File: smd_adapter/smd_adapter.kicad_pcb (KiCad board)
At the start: 2 copper layers, 7.7 x 7.7 mm, 6 parts, among them J1 Conn_01x01_Pin, J2 Conn_01x01_Pin, J3 Conn_01x01_Pin, J4 Conn_01x01_Pin, J5 Conn_01x01_Pin, U2 MCP73831-5-OT

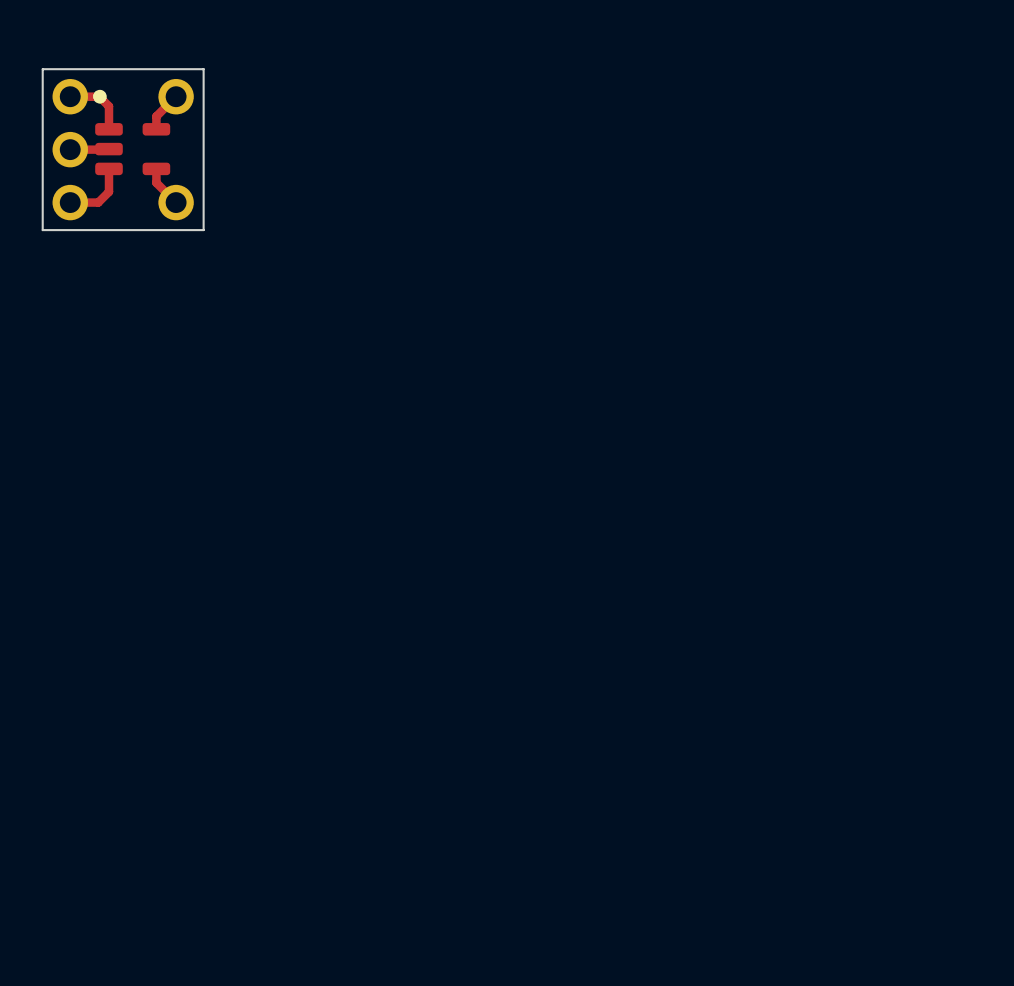
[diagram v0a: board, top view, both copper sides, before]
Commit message: Created adapter panel (5 x 5)
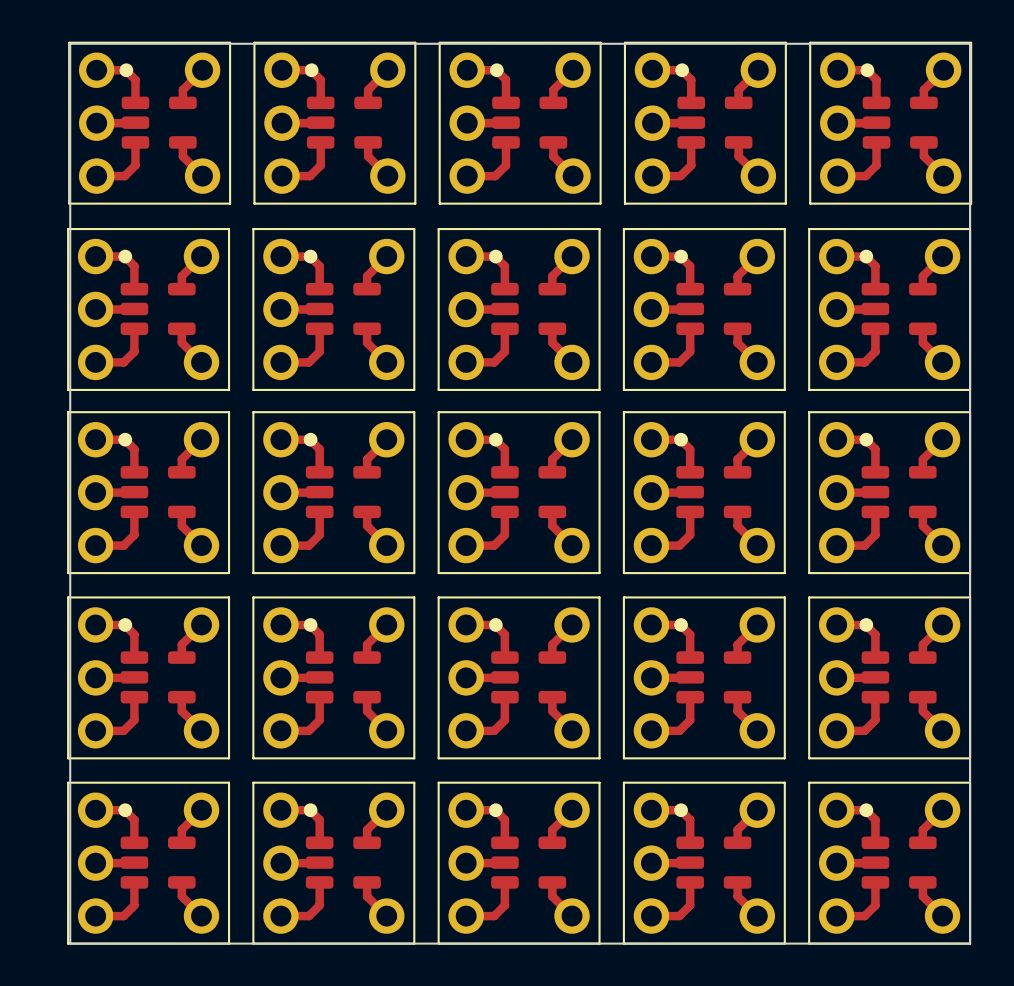
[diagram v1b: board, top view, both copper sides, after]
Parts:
- added J1: Conn_01x01_Pin, smd_adapter:pin_pad, F.Cu at (158.7, 143.5)
- added J1: Conn_01x01_Pin, smd_adapter:pin_pad, F.Cu at (194.3, 134.6)
- added J1: Conn_01x01_Pin, smd_adapter:pin_pad, F.Cu at (185.4, 134.6)
- added J1: Conn_01x01_Pin, smd_adapter:pin_pad, F.Cu at (185.4, 125.7)
- added J1: Conn_01x01_Pin, smd_adapter:pin_pad, F.Cu at (185.4, 108.0)
- added J1: Conn_01x01_Pin, smd_adapter:pin_pad, F.Cu at (167.6, 125.7)
- added J1: Conn_01x01_Pin, smd_adapter:pin_pad, F.Cu at (176.5, 143.5)
- added J1: Conn_01x01_Pin, smd_adapter:pin_pad, F.Cu at (176.5, 125.7)
- added J1: Conn_01x01_Pin, smd_adapter:pin_pad, F.Cu at (167.6, 143.5)
- added J1: Conn_01x01_Pin, smd_adapter:pin_pad, F.Cu at (176.5, 134.6)
- added J1: Conn_01x01_Pin, smd_adapter:pin_pad, F.Cu at (194.3, 125.7)
- added J1: Conn_01x01_Pin, smd_adapter:pin_pad, F.Cu at (167.6, 108.0)
- added J1: Conn_01x01_Pin, smd_adapter:pin_pad, F.Cu at (185.4, 116.9)
- added J1: Conn_01x01_Pin, smd_adapter:pin_pad, F.Cu at (158.7, 134.6)
- added J1: Conn_01x01_Pin, smd_adapter:pin_pad, F.Cu at (158.7, 125.7)
- added J1: Conn_01x01_Pin, smd_adapter:pin_pad, F.Cu at (194.3, 116.9)
- added J1: Conn_01x01_Pin, smd_adapter:pin_pad, F.Cu at (167.6, 134.6)
- added J1: Conn_01x01_Pin, smd_adapter:pin_pad, F.Cu at (194.3, 108.0)
- added J1: Conn_01x01_Pin, smd_adapter:pin_pad, F.Cu at (176.5, 116.9)
- added J1: Conn_01x01_Pin, smd_adapter:pin_pad, F.Cu at (167.6, 116.9)
- added J1: Conn_01x01_Pin, smd_adapter:pin_pad, F.Cu at (194.3, 143.5)
- added J1: Conn_01x01_Pin, smd_adapter:pin_pad, F.Cu at (185.4, 143.5)
- added J1: Conn_01x01_Pin, smd_adapter:pin_pad, F.Cu at (158.7, 116.9)
- added J1: Conn_01x01_Pin, smd_adapter:pin_pad, F.Cu at (176.5, 108.0)
- added J2: Conn_01x01_Pin, smd_adapter:pin_pad, F.Cu at (167.6, 129.5)
- added J2: Conn_01x01_Pin, smd_adapter:pin_pad, F.Cu at (158.7, 120.6)
- added J2: Conn_01x01_Pin, smd_adapter:pin_pad, F.Cu at (158.7, 111.8)
- added J2: Conn_01x01_Pin, smd_adapter:pin_pad, F.Cu at (167.6, 120.6)
- added J2: Conn_01x01_Pin, smd_adapter:pin_pad, F.Cu at (185.4, 102.9)
- added J2: Conn_01x01_Pin, smd_adapter:pin_pad, F.Cu at (194.3, 102.9)
- added J2: Conn_01x01_Pin, smd_adapter:pin_pad, F.Cu at (176.5, 138.4)
- added J2: Conn_01x01_Pin, smd_adapter:pin_pad, F.Cu at (176.5, 102.9)
- added J2: Conn_01x01_Pin, smd_adapter:pin_pad, F.Cu at (185.4, 120.6)
- added J2: Conn_01x01_Pin, smd_adapter:pin_pad, F.Cu at (158.7, 138.4)
- added J2: Conn_01x01_Pin, smd_adapter:pin_pad, F.Cu at (176.5, 111.8)
- added J2: Conn_01x01_Pin, smd_adapter:pin_pad, F.Cu at (167.6, 111.8)
- added J2: Conn_01x01_Pin, smd_adapter:pin_pad, F.Cu at (194.3, 120.6)
- added J2: Conn_01x01_Pin, smd_adapter:pin_pad, F.Cu at (176.5, 120.6)
- added J2: Conn_01x01_Pin, smd_adapter:pin_pad, F.Cu at (185.4, 129.5)
- added J2: Conn_01x01_Pin, smd_adapter:pin_pad, F.Cu at (167.6, 102.9)
- added J2: Conn_01x01_Pin, smd_adapter:pin_pad, F.Cu at (194.3, 111.8)
- added J2: Conn_01x01_Pin, smd_adapter:pin_pad, F.Cu at (158.7, 129.5)
- added J2: Conn_01x01_Pin, smd_adapter:pin_pad, F.Cu at (194.3, 129.5)
- added J2: Conn_01x01_Pin, smd_adapter:pin_pad, F.Cu at (185.4, 138.4)
- added J2: Conn_01x01_Pin, smd_adapter:pin_pad, F.Cu at (194.3, 138.4)
- added J2: Conn_01x01_Pin, smd_adapter:pin_pad, F.Cu at (176.5, 129.5)
- added J2: Conn_01x01_Pin, smd_adapter:pin_pad, F.Cu at (185.4, 111.8)
- added J2: Conn_01x01_Pin, smd_adapter:pin_pad, F.Cu at (167.6, 138.4)
- added J3: Conn_01x01_Pin, smd_adapter:pin_pad, F.Cu at (189.2, 114.4)
- added J3: Conn_01x01_Pin, smd_adapter:pin_pad, F.Cu at (153.6, 123.1)
- added J3: Conn_01x01_Pin, smd_adapter:pin_pad, F.Cu at (180.3, 140.9)
- added J3: Conn_01x01_Pin, smd_adapter:pin_pad, F.Cu at (162.6, 105.4)
- added J3: Conn_01x01_Pin, smd_adapter:pin_pad, F.Cu at (180.3, 114.4)
- added J3: Conn_01x01_Pin, smd_adapter:pin_pad, F.Cu at (171.4, 114.4)
- added J3: Conn_01x01_Pin, smd_adapter:pin_pad, F.Cu at (171.4, 132.0)
- added J3: Conn_01x01_Pin, smd_adapter:pin_pad, F.Cu at (189.2, 123.1)
- added J3: Conn_01x01_Pin, smd_adapter:pin_pad, F.Cu at (162.5, 132.0)
- added J3: Conn_01x01_Pin, smd_adapter:pin_pad, F.Cu at (162.5, 123.1)
- added J3: Conn_01x01_Pin, smd_adapter:pin_pad, F.Cu at (171.4, 105.4)
- added J3: Conn_01x01_Pin, smd_adapter:pin_pad, F.Cu at (180.3, 105.4)
- added J3: Conn_01x01_Pin, smd_adapter:pin_pad, F.Cu at (189.2, 140.9)
- added J3: Conn_01x01_Pin, smd_adapter:pin_pad, F.Cu at (153.6, 114.4)
- added J3: Conn_01x01_Pin, smd_adapter:pin_pad, F.Cu at (189.2, 105.4)
- added J3: Conn_01x01_Pin, smd_adapter:pin_pad, F.Cu at (162.5, 140.9)
- added J3: Conn_01x01_Pin, smd_adapter:pin_pad, F.Cu at (153.6, 132.0)
- added J3: Conn_01x01_Pin, smd_adapter:pin_pad, F.Cu at (162.5, 114.4)
- added J3: Conn_01x01_Pin, smd_adapter:pin_pad, F.Cu at (180.3, 123.1)
- added J3: Conn_01x01_Pin, smd_adapter:pin_pad, F.Cu at (171.4, 123.1)
- added J3: Conn_01x01_Pin, smd_adapter:pin_pad, F.Cu at (153.6, 140.9)
- added J3: Conn_01x01_Pin, smd_adapter:pin_pad, F.Cu at (189.2, 132.0)
- added J3: Conn_01x01_Pin, smd_adapter:pin_pad, F.Cu at (171.4, 140.9)
- added J3: Conn_01x01_Pin, smd_adapter:pin_pad, F.Cu at (180.3, 132.0)
- added J4: Conn_01x01_Pin, smd_adapter:pin_pad, F.Cu at (153.6, 138.4)
- added J4: Conn_01x01_Pin, smd_adapter:pin_pad, F.Cu at (171.4, 111.8)
- added J4: Conn_01x01_Pin, smd_adapter:pin_pad, F.Cu at (171.4, 120.6)
- added J4: Conn_01x01_Pin, smd_adapter:pin_pad, F.Cu at (171.4, 129.5)
- added J4: Conn_01x01_Pin, smd_adapter:pin_pad, F.Cu at (162.6, 102.9)
- added J4: Conn_01x01_Pin, smd_adapter:pin_pad, F.Cu at (162.5, 129.5)
- added J4: Conn_01x01_Pin, smd_adapter:pin_pad, F.Cu at (189.2, 138.4)
- added J4: Conn_01x01_Pin, smd_adapter:pin_pad, F.Cu at (153.6, 111.8)
- added J4: Conn_01x01_Pin, smd_adapter:pin_pad, F.Cu at (180.3, 120.6)
- added J4: Conn_01x01_Pin, smd_adapter:pin_pad, F.Cu at (171.4, 102.9)
- added J4: Conn_01x01_Pin, smd_adapter:pin_pad, F.Cu at (180.3, 138.4)
- added J4: Conn_01x01_Pin, smd_adapter:pin_pad, F.Cu at (189.2, 102.9)
- added J4: Conn_01x01_Pin, smd_adapter:pin_pad, F.Cu at (153.6, 120.6)
- added J4: Conn_01x01_Pin, smd_adapter:pin_pad, F.Cu at (180.3, 129.5)
- added J4: Conn_01x01_Pin, smd_adapter:pin_pad, F.Cu at (162.5, 120.6)
- added J4: Conn_01x01_Pin, smd_adapter:pin_pad, F.Cu at (180.3, 111.8)
- added J4: Conn_01x01_Pin, smd_adapter:pin_pad, F.Cu at (153.6, 129.5)
- added J4: Conn_01x01_Pin, smd_adapter:pin_pad, F.Cu at (189.2, 111.8)
- added J4: Conn_01x01_Pin, smd_adapter:pin_pad, F.Cu at (162.5, 111.8)
- added J4: Conn_01x01_Pin, smd_adapter:pin_pad, F.Cu at (189.2, 120.6)
- added J4: Conn_01x01_Pin, smd_adapter:pin_pad, F.Cu at (171.4, 138.4)
- added J4: Conn_01x01_Pin, smd_adapter:pin_pad, F.Cu at (189.2, 129.5)
- added J4: Conn_01x01_Pin, smd_adapter:pin_pad, F.Cu at (162.5, 138.4)
- added J4: Conn_01x01_Pin, smd_adapter:pin_pad, F.Cu at (180.3, 102.9)
- added J5: Conn_01x01_Pin, smd_adapter:pin_pad, F.Cu at (171.4, 116.9)
- added J5: Conn_01x01_Pin, smd_adapter:pin_pad, F.Cu at (153.6, 125.7)
- added J5: Conn_01x01_Pin, smd_adapter:pin_pad, F.Cu at (162.6, 108.0)
- added J5: Conn_01x01_Pin, smd_adapter:pin_pad, F.Cu at (189.2, 143.5)
- added J5: Conn_01x01_Pin, smd_adapter:pin_pad, F.Cu at (180.3, 143.5)
- added J5: Conn_01x01_Pin, smd_adapter:pin_pad, F.Cu at (153.6, 143.5)
- added J5: Conn_01x01_Pin, smd_adapter:pin_pad, F.Cu at (189.2, 134.6)
- added J5: Conn_01x01_Pin, smd_adapter:pin_pad, F.Cu at (171.4, 125.7)
- added J5: Conn_01x01_Pin, smd_adapter:pin_pad, F.Cu at (180.3, 134.6)
- added J5: Conn_01x01_Pin, smd_adapter:pin_pad, F.Cu at (189.2, 116.9)
- added J5: Conn_01x01_Pin, smd_adapter:pin_pad, F.Cu at (171.4, 134.6)
- added J5: Conn_01x01_Pin, smd_adapter:pin_pad, F.Cu at (153.6, 134.6)
- added J5: Conn_01x01_Pin, smd_adapter:pin_pad, F.Cu at (162.5, 143.5)
- added J5: Conn_01x01_Pin, smd_adapter:pin_pad, F.Cu at (180.3, 116.9)
- added J5: Conn_01x01_Pin, smd_adapter:pin_pad, F.Cu at (189.2, 108.0)
- added J5: Conn_01x01_Pin, smd_adapter:pin_pad, F.Cu at (171.4, 143.5)
- added J5: Conn_01x01_Pin, smd_adapter:pin_pad, F.Cu at (162.5, 116.9)
- added J5: Conn_01x01_Pin, smd_adapter:pin_pad, F.Cu at (180.3, 108.0)
- added J5: Conn_01x01_Pin, smd_adapter:pin_pad, F.Cu at (189.2, 125.7)
- added J5: Conn_01x01_Pin, smd_adapter:pin_pad, F.Cu at (171.4, 108.0)
- added J5: Conn_01x01_Pin, smd_adapter:pin_pad, F.Cu at (162.5, 125.7)
- added J5: Conn_01x01_Pin, smd_adapter:pin_pad, F.Cu at (180.3, 125.7)
- added J5: Conn_01x01_Pin, smd_adapter:pin_pad, F.Cu at (153.6, 116.9)
- added J5: Conn_01x01_Pin, smd_adapter:pin_pad, F.Cu at (162.5, 134.6)
- added U2: MCP73831-5-OT, smd_adapter:SOT-23-5, F.Cu at (156.6, 123.1)
- added U2: MCP73831-5-OT, smd_adapter:SOT-23-5, F.Cu at (156.6, 114.3)
- added U2: MCP73831-5-OT, smd_adapter:SOT-23-5, F.Cu at (183.3, 132.0)
- added U2: MCP73831-5-OT, smd_adapter:SOT-23-5, F.Cu at (165.6, 105.4)
- added U2: MCP73831-5-OT, smd_adapter:SOT-23-5, F.Cu at (183.3, 140.9)
- added U2: MCP73831-5-OT, smd_adapter:SOT-23-5, F.Cu at (156.6, 140.9)
- added U2: MCP73831-5-OT, smd_adapter:SOT-23-5, F.Cu at (183.3, 114.3)
- added U2: MCP73831-5-OT, smd_adapter:SOT-23-5, F.Cu at (192.2, 114.3)
- added U2: MCP73831-5-OT, smd_adapter:SOT-23-5, F.Cu at (174.4, 123.1)
- added U2: MCP73831-5-OT, smd_adapter:SOT-23-5, F.Cu at (192.2, 140.9)
- added U2: MCP73831-5-OT, smd_adapter:SOT-23-5, F.Cu at (174.4, 132.0)
- added U2: MCP73831-5-OT, smd_adapter:SOT-23-5, F.Cu at (192.2, 123.1)
- added U2: MCP73831-5-OT, smd_adapter:SOT-23-5, F.Cu at (165.5, 123.1)
- added U2: MCP73831-5-OT, smd_adapter:SOT-23-5, F.Cu at (165.5, 140.9)
- added U2: MCP73831-5-OT, smd_adapter:SOT-23-5, F.Cu at (174.4, 114.3)
- added U2: MCP73831-5-OT, smd_adapter:SOT-23-5, F.Cu at (192.2, 105.4)
- added U2: MCP73831-5-OT, smd_adapter:SOT-23-5, F.Cu at (165.5, 114.3)
- added U2: MCP73831-5-OT, smd_adapter:SOT-23-5, F.Cu at (183.3, 123.1)
- added U2: MCP73831-5-OT, smd_adapter:SOT-23-5, F.Cu at (165.5, 132.0)
- added U2: MCP73831-5-OT, smd_adapter:SOT-23-5, F.Cu at (174.4, 105.4)
- added U2: MCP73831-5-OT, smd_adapter:SOT-23-5, F.Cu at (183.3, 105.4)
- added U2: MCP73831-5-OT, smd_adapter:SOT-23-5, F.Cu at (192.2, 132.0)
- added U2: MCP73831-5-OT, smd_adapter:SOT-23-5, F.Cu at (174.4, 140.9)
- added U2: MCP73831-5-OT, smd_adapter:SOT-23-5, F.Cu at (156.6, 132.0)
- moved J1 1.80 mm to (158.8, 108.0)
- moved J2 1.80 mm to (158.8, 102.9)
- moved U2 1.80 mm to (156.7, 105.4)
- moved J3 1.80 mm to (153.7, 105.4)
- moved J4 1.80 mm to (153.7, 102.9)
- moved J5 1.80 mm to (153.7, 108.0)
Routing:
- net Net-(J5-Pin_1): track 3.17 -> 79.4 mm
- net Net-(J4-Pin_1): track 3.15 -> 78.8 mm
- net Net-(J1-Pin_1): track 2.01 -> 50.2 mm
- net Net-(J2-Pin_1): track 1.96 -> 48.9 mm
- net Net-(J3-Pin_1): track 1.87 -> 46.8 mm
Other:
- board size 7.7 x 7.7 mm -> 43.2 x 43.2 mm

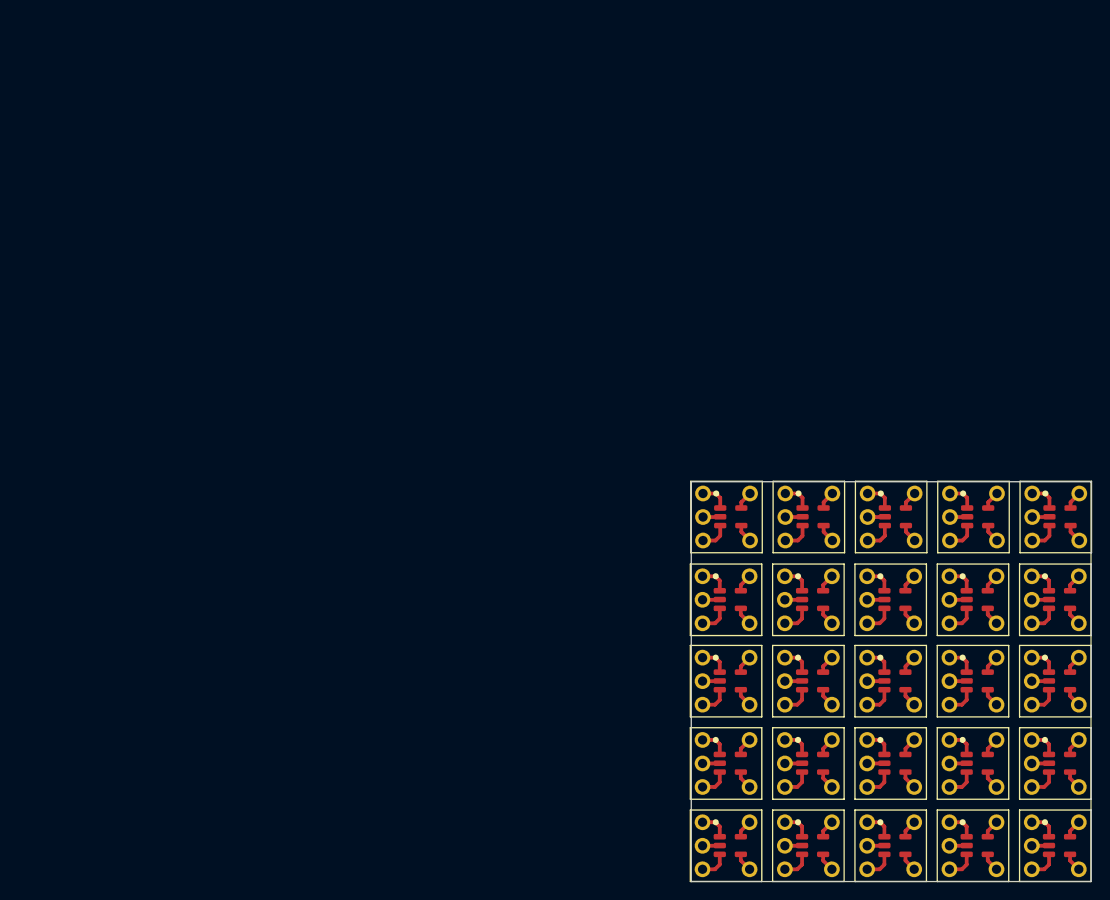
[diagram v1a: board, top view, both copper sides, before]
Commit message: Completed the layout of the smd adapters (5 kinds)
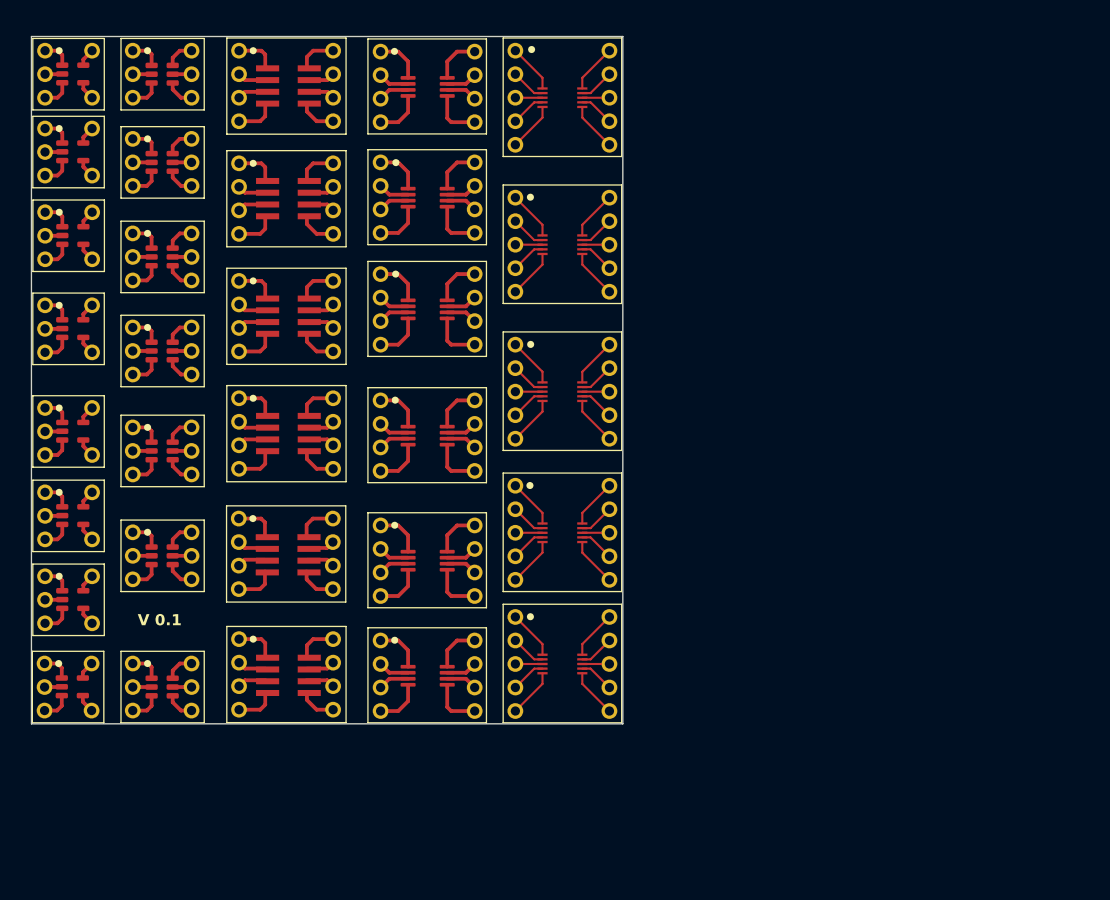
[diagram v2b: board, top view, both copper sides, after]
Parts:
- removed the J1 at (158.7, 143.5)
- removed the J1 at (194.3, 134.6)
- removed the J1 at (185.4, 134.6)
- removed the J1 at (185.4, 125.7)
- removed the J1 at (185.4, 108.0)
- removed the J1 at (167.6, 125.7)
- removed the J1 at (176.5, 143.5)
- removed the J1 at (176.5, 125.7)
- removed the J1 at (167.6, 143.5)
- removed the J1 at (176.5, 134.6)
- removed the J1 at (194.3, 125.7)
- removed the J1 at (167.6, 108.0)
- removed the J1 at (185.4, 116.9)
- removed the J1 at (158.7, 134.6)
- removed the J1 at (158.7, 125.7)
- removed the J1 at (194.3, 116.9)
- removed the J1 at (167.6, 134.6)
- removed the J1 at (194.3, 108.0)
- removed the J1 at (176.5, 116.9)
- removed the J1 at (167.6, 116.9)
- removed the J1 at (194.3, 143.5)
- removed the J1 at (185.4, 143.5)
- removed the J1 at (158.7, 116.9)
- removed the J1 at (176.5, 108.0)
- removed the J2 at (167.6, 129.5)
- removed the J2 at (158.7, 120.6)
- removed the J2 at (158.7, 111.8)
- removed the J2 at (167.6, 120.6)
- removed the J2 at (185.4, 102.9)
- removed the J2 at (194.3, 102.9)
- removed the J2 at (176.5, 138.4)
- removed the J2 at (176.5, 102.9)
- removed the J2 at (185.4, 120.6)
- removed the J2 at (158.7, 138.4)
- removed the J2 at (176.5, 111.8)
- removed the J2 at (167.6, 111.8)
- removed the J2 at (194.3, 120.6)
- removed the J2 at (176.5, 120.6)
- removed the J2 at (185.4, 129.5)
- removed the J2 at (167.6, 102.9)
- removed the J2 at (194.3, 111.8)
- removed the J2 at (158.7, 129.5)
- removed the J2 at (194.3, 129.5)
- removed the J2 at (185.4, 138.4)
- removed the J2 at (194.3, 138.4)
- removed the J2 at (176.5, 129.5)
- removed the J2 at (185.4, 111.8)
- removed the J2 at (167.6, 138.4)
- removed the J3 at (189.2, 114.4)
- removed the J3 at (153.6, 123.1)
- removed the J3 at (180.3, 140.9)
- removed the J3 at (162.6, 105.4)
- removed the J3 at (180.3, 114.4)
- removed the J3 at (171.4, 114.4)
- removed the J3 at (171.4, 132.0)
- removed the J3 at (189.2, 123.1)
- removed the J3 at (162.5, 132.0)
- removed the J3 at (162.5, 123.1)
- removed the J3 at (171.4, 105.4)
- removed the J3 at (180.3, 105.4)
- removed the J3 at (189.2, 140.9)
- removed the J3 at (153.6, 114.4)
- removed the J3 at (189.2, 105.4)
- removed the J3 at (162.5, 140.9)
- removed the J3 at (153.6, 132.0)
- removed the J3 at (162.5, 114.4)
- removed the J3 at (180.3, 123.1)
- removed the J3 at (171.4, 123.1)
- removed the J3 at (153.6, 140.9)
- removed the J3 at (189.2, 132.0)
- removed the J3 at (171.4, 140.9)
- removed the J3 at (180.3, 132.0)
- removed the J4 at (153.6, 138.4)
- removed the J4 at (171.4, 111.8)
- removed the J4 at (171.4, 120.6)
- removed the J4 at (171.4, 129.5)
- removed the J4 at (162.6, 102.9)
- removed the J4 at (162.5, 129.5)
- removed the J4 at (189.2, 138.4)
- removed the J4 at (153.6, 111.8)
- removed the J4 at (180.3, 120.6)
- removed the J4 at (171.4, 102.9)
- removed the J4 at (180.3, 138.4)
- removed the J4 at (189.2, 102.9)
- removed the J4 at (153.6, 120.6)
- removed the J4 at (180.3, 129.5)
- removed the J4 at (162.5, 120.6)
- removed the J4 at (180.3, 111.8)
- removed the J4 at (153.6, 129.5)
- removed the J4 at (189.2, 111.8)
- removed the J4 at (162.5, 111.8)
- removed the J4 at (189.2, 120.6)
- removed the J4 at (171.4, 138.4)
- removed the J4 at (189.2, 129.5)
- removed the J4 at (162.5, 138.4)
- removed the J4 at (180.3, 102.9)
- removed the J5 at (171.4, 116.9)
- removed the J5 at (153.6, 125.7)
- removed the J5 at (162.6, 108.0)
- removed the J5 at (189.2, 143.5)
- removed the J5 at (180.3, 143.5)
- removed the J5 at (153.6, 143.5)
- removed the J5 at (189.2, 134.6)
- removed the J5 at (171.4, 125.7)
- removed the J5 at (180.3, 134.6)
- removed the J5 at (189.2, 116.9)
- removed the J5 at (171.4, 134.6)
- removed the J5 at (153.6, 134.6)
- removed the J5 at (162.5, 143.5)
- removed the J5 at (180.3, 116.9)
- removed the J5 at (189.2, 108.0)
- removed the J5 at (171.4, 143.5)
- removed the J5 at (162.5, 116.9)
- removed the J5 at (180.3, 108.0)
- removed the J5 at (189.2, 125.7)
- removed the J5 at (171.4, 108.0)
- removed the J5 at (162.5, 125.7)
- removed the J5 at (180.3, 125.7)
- removed the J5 at (153.6, 116.9)
- removed the J5 at (162.5, 134.6)
- removed the U2 at (156.6, 123.1)
- removed the U2 at (156.6, 114.3)
- removed the U2 at (183.3, 132.0)
- removed the U2 at (165.6, 105.4)
- removed the U2 at (183.3, 140.9)
- removed the U2 at (156.6, 140.9)
- removed the U2 at (183.3, 114.3)
- removed the U2 at (192.2, 114.3)
- removed the U2 at (174.4, 123.1)
- removed the U2 at (192.2, 140.9)
- removed the U2 at (174.4, 132.0)
- removed the U2 at (192.2, 123.1)
- removed the U2 at (165.5, 123.1)
- removed the U2 at (165.5, 140.9)
- removed the U2 at (174.4, 114.3)
- removed the U2 at (192.2, 105.4)
- removed the U2 at (165.5, 114.3)
- removed the U2 at (183.3, 123.1)
- removed the U2 at (165.5, 132.0)
- removed the U2 at (174.4, 105.4)
- removed the U2 at (183.3, 105.4)
- removed the U2 at (192.2, 132.0)
- removed the U2 at (174.4, 140.9)
- removed the U2 at (156.6, 132.0)
- added J1: Conn_01x01_Pin, smd_adapter:pin_pad, F.Cu at (87.7, 107.8)
- added J1: Conn_01x01_Pin, smd_adapter:pin_pad, F.Cu at (87.6, 126.3)
- added J1: Conn_01x01_Pin, smd_adapter:pin_pad, F.Cu at (87.7, 87.6)
- added J1: Conn_01x01_Pin, smd_adapter:pin_pad, F.Cu at (87.7, 68.5)
- added J1: Conn_01x01_Pin, smd_adapter:pin_pad, F.Cu at (87.7, 98.7)
- added J1: Conn_01x01_Pin, smd_adapter:pin_pad, F.Cu at (87.7, 116.9)
- added J1: Conn_01x01_Pin, smd_adapter:pin_pad, F.Cu at (87.7, 77.6)
- added J10: Conn_01x01_Pin, smd_adapter:pin_pad, F.Cu at (113.7, 105.6)
- added J10: Conn_01x01_Pin, smd_adapter:pin_pad, F.Cu at (113.7, 118.6)
- added J10: Conn_01x01_Pin, smd_adapter:pin_pad, F.Cu at (113.7, 79.9)
- added J10: Conn_01x01_Pin, smd_adapter:pin_pad, F.Cu at (113.7, 92.6)
- added J10: Conn_01x01_Pin, smd_adapter:pin_pad, F.Cu at (113.7, 55.0)
- added J10: Conn_01x01_Pin, smd_adapter:pin_pad, F.Cu at (113.7, 67.2)
- added J11: Conn_01x01_Pin, smd_adapter:pin_pad, F.Cu at (113.7, 82.4)
- added J11: Conn_01x01_Pin, smd_adapter:pin_pad, F.Cu at (113.7, 95.1)
- added J11: Conn_01x01_Pin, smd_adapter:pin_pad, F.Cu at (113.7, 57.6)
- added J11: Conn_01x01_Pin, smd_adapter:pin_pad, F.Cu at (113.7, 69.7)
- added J11: Conn_01x01_Pin, smd_adapter:pin_pad, F.Cu at (113.7, 121.1)
- added J11: Conn_01x01_Pin, smd_adapter:pin_pad, F.Cu at (113.7, 108.1)
- added J12: Conn_01x01_Pin, smd_adapter:pin_pad, F.Cu at (113.7, 110.7)
- added J12: Conn_01x01_Pin, smd_adapter:pin_pad, F.Cu at (113.7, 60.1)
- added J12: Conn_01x01_Pin, smd_adapter:pin_pad, F.Cu at (113.7, 85.0)
- added J12: Conn_01x01_Pin, smd_adapter:pin_pad, F.Cu at (113.7, 97.7)
- added J12: Conn_01x01_Pin, smd_adapter:pin_pad, F.Cu at (113.7, 72.3)
- added J12: Conn_01x01_Pin, smd_adapter:pin_pad, F.Cu at (113.7, 123.7)
- added J13: Conn_01x01_Pin, smd_adapter:pin_pad, F.Cu at (113.7, 113.2)
- added J13: Conn_01x01_Pin, smd_adapter:pin_pad, F.Cu at (113.7, 87.5)
- added J13: Conn_01x01_Pin, smd_adapter:pin_pad, F.Cu at (113.7, 62.7)
- added J13: Conn_01x01_Pin, smd_adapter:pin_pad, F.Cu at (113.7, 74.8)
- added J13: Conn_01x01_Pin, smd_adapter:pin_pad, F.Cu at (113.7, 100.2)
- added J13: Conn_01x01_Pin, smd_adapter:pin_pad, F.Cu at (113.7, 126.2)
- added J14: Conn_01x01_Pin, smd_adapter:pin_pad, F.Cu at (92.1, 121.2)
- added J14: Conn_01x01_Pin, smd_adapter:pin_pad, F.Cu at (92.1, 64.6)
- added J14: Conn_01x01_Pin, smd_adapter:pin_pad, F.Cu at (92.1, 95.7)
- added J14: Conn_01x01_Pin, smd_adapter:pin_pad, F.Cu at (92.1, 107.1)
- added J14: Conn_01x01_Pin, smd_adapter:pin_pad, F.Cu at (92.1, 55.0)
- added J14: Conn_01x01_Pin, smd_adapter:pin_pad, F.Cu at (92.1, 74.8)
- added J14: Conn_01x01_Pin, smd_adapter:pin_pad, F.Cu at (92.1, 84.9)
- added J15: Conn_01x01_Pin, smd_adapter:pin_pad, F.Cu at (92.1, 98.3)
- added J15: Conn_01x01_Pin, smd_adapter:pin_pad, F.Cu at (92.1, 57.6)
- added J15: Conn_01x01_Pin, smd_adapter:pin_pad, F.Cu at (92.1, 109.6)
- added J15: Conn_01x01_Pin, smd_adapter:pin_pad, F.Cu at (92.1, 123.8)
- added J15: Conn_01x01_Pin, smd_adapter:pin_pad, F.Cu at (92.1, 77.3)
- added J15: Conn_01x01_Pin, smd_adapter:pin_pad, F.Cu at (92.1, 87.5)
- added J15: Conn_01x01_Pin, smd_adapter:pin_pad, F.Cu at (92.1, 67.1)
- added J16: Conn_01x01_Pin, smd_adapter:pin_pad, F.Cu at (92.1, 112.1)
- added J16: Conn_01x01_Pin, smd_adapter:pin_pad, F.Cu at (92.1, 126.3)
- added J16: Conn_01x01_Pin, smd_adapter:pin_pad, F.Cu at (92.1, 69.6)
- added J16: Conn_01x01_Pin, smd_adapter:pin_pad, F.Cu at (92.1, 90.0)
- added J16: Conn_01x01_Pin, smd_adapter:pin_pad, F.Cu at (92.1, 79.9)
- added J16: Conn_01x01_Pin, smd_adapter:pin_pad, F.Cu at (92.1, 60.1)
- added J16: Conn_01x01_Pin, smd_adapter:pin_pad, F.Cu at (92.1, 100.8)
- added J17: Conn_01x01_Pin, smd_adapter:pin_pad, F.Cu at (98.4, 74.8)
- added J17: Conn_01x01_Pin, smd_adapter:pin_pad, F.Cu at (98.4, 121.2)
- added J17: Conn_01x01_Pin, smd_adapter:pin_pad, F.Cu at (98.4, 55.0)
- added J17: Conn_01x01_Pin, smd_adapter:pin_pad, F.Cu at (98.4, 95.7)
- added J17: Conn_01x01_Pin, smd_adapter:pin_pad, F.Cu at (98.4, 84.9)
- added J17: Conn_01x01_Pin, smd_adapter:pin_pad, F.Cu at (98.4, 64.6)
- added J17: Conn_01x01_Pin, smd_adapter:pin_pad, F.Cu at (98.4, 107.1)
- added J18: Conn_01x01_Pin, smd_adapter:pin_pad, F.Cu at (98.4, 109.6)
- added J18: Conn_01x01_Pin, smd_adapter:pin_pad, F.Cu at (98.4, 57.6)
- added J18: Conn_01x01_Pin, smd_adapter:pin_pad, F.Cu at (98.4, 77.3)
- added J18: Conn_01x01_Pin, smd_adapter:pin_pad, F.Cu at (98.4, 98.3)
- added J18: Conn_01x01_Pin, smd_adapter:pin_pad, F.Cu at (98.4, 123.8)
- added J18: Conn_01x01_Pin, smd_adapter:pin_pad, F.Cu at (98.4, 87.5)
- added J18: Conn_01x01_Pin, smd_adapter:pin_pad, F.Cu at (98.4, 67.1)
- added J19: Conn_01x01_Pin, smd_adapter:pin_pad, F.Cu at (98.4, 100.8)
- added J19: Conn_01x01_Pin, smd_adapter:pin_pad, F.Cu at (98.4, 126.3)
- added J19: Conn_01x01_Pin, smd_adapter:pin_pad, F.Cu at (98.4, 79.9)
- added J19: Conn_01x01_Pin, smd_adapter:pin_pad, F.Cu at (98.4, 60.1)
- added J19: Conn_01x01_Pin, smd_adapter:pin_pad, F.Cu at (98.4, 69.6)
- added J19: Conn_01x01_Pin, smd_adapter:pin_pad, F.Cu at (98.4, 90.0)
- added J19: Conn_01x01_Pin, smd_adapter:pin_pad, F.Cu at (98.4, 112.1)
- added J2: Conn_01x01_Pin, smd_adapter:pin_pad, F.Cu at (87.7, 72.5)
- added J2: Conn_01x01_Pin, smd_adapter:pin_pad, F.Cu at (87.7, 82.5)
- added J2: Conn_01x01_Pin, smd_adapter:pin_pad, F.Cu at (87.7, 63.4)
- added J2: Conn_01x01_Pin, smd_adapter:pin_pad, F.Cu at (87.7, 93.6)
- added J2: Conn_01x01_Pin, smd_adapter:pin_pad, F.Cu at (87.6, 121.2)
- added J2: Conn_01x01_Pin, smd_adapter:pin_pad, F.Cu at (87.7, 102.7)
- added J2: Conn_01x01_Pin, smd_adapter:pin_pad, F.Cu at (87.7, 111.8)
- added J20: Conn_01x01_Pin, smd_adapter:pin_pad, F.Cu at (118.8, 79.2)
- added J20: Conn_01x01_Pin, smd_adapter:pin_pad, F.Cu at (118.8, 55.1)
- added J20: Conn_01x01_Pin, smd_adapter:pin_pad, F.Cu at (118.8, 67.1)
- added J20: Conn_01x01_Pin, smd_adapter:pin_pad, F.Cu at (118.8, 118.7)
- added J20: Conn_01x01_Pin, smd_adapter:pin_pad, F.Cu at (118.8, 106.3)
- added J20: Conn_01x01_Pin, smd_adapter:pin_pad, F.Cu at (118.8, 92.8)
- added J21: Conn_01x01_Pin, smd_adapter:pin_pad, F.Cu at (118.8, 81.7)
- added J21: Conn_01x01_Pin, smd_adapter:pin_pad, F.Cu at (118.8, 57.7)
- added J21: Conn_01x01_Pin, smd_adapter:pin_pad, F.Cu at (118.8, 69.6)
- added J21: Conn_01x01_Pin, smd_adapter:pin_pad, F.Cu at (118.8, 108.9)
- added J21: Conn_01x01_Pin, smd_adapter:pin_pad, F.Cu at (118.8, 95.4)
- added J21: Conn_01x01_Pin, smd_adapter:pin_pad, F.Cu at (118.8, 121.3)
- added J22: Conn_01x01_Pin, smd_adapter:pin_pad, F.Cu at (118.8, 123.8)
- added J22: Conn_01x01_Pin, smd_adapter:pin_pad, F.Cu at (118.8, 111.4)
- added J22: Conn_01x01_Pin, smd_adapter:pin_pad, F.Cu at (118.8, 60.2)
- added J22: Conn_01x01_Pin, smd_adapter:pin_pad, F.Cu at (118.8, 97.9)
- added J22: Conn_01x01_Pin, smd_adapter:pin_pad, F.Cu at (118.8, 84.3)
- added J22: Conn_01x01_Pin, smd_adapter:pin_pad, F.Cu at (118.8, 72.2)
- added J23: Conn_01x01_Pin, smd_adapter:pin_pad, F.Cu at (118.8, 62.8)
- added J23: Conn_01x01_Pin, smd_adapter:pin_pad, F.Cu at (118.8, 126.4)
- added J23: Conn_01x01_Pin, smd_adapter:pin_pad, F.Cu at (118.8, 74.7)
- added J23: Conn_01x01_Pin, smd_adapter:pin_pad, F.Cu at (118.8, 86.8)
- added J23: Conn_01x01_Pin, smd_adapter:pin_pad, F.Cu at (118.8, 100.4)
- added J23: Conn_01x01_Pin, smd_adapter:pin_pad, F.Cu at (118.8, 113.9)
- added J24: Conn_01x01_Pin, smd_adapter:pin_pad, F.Cu at (129.0, 118.7)
- added J24: Conn_01x01_Pin, smd_adapter:pin_pad, F.Cu at (129.0, 55.1)
- added J24: Conn_01x01_Pin, smd_adapter:pin_pad, F.Cu at (129.0, 67.1)
- added J24: Conn_01x01_Pin, smd_adapter:pin_pad, F.Cu at (129.0, 106.3)
- added J24: Conn_01x01_Pin, smd_adapter:pin_pad, F.Cu at (129.0, 79.2)
- added J24: Conn_01x01_Pin, smd_adapter:pin_pad, F.Cu at (129.0, 92.8)
- added J25: Conn_01x01_Pin, smd_adapter:pin_pad, F.Cu at (129.0, 81.7)
- added J25: Conn_01x01_Pin, smd_adapter:pin_pad, F.Cu at (129.0, 95.4)
- added J25: Conn_01x01_Pin, smd_adapter:pin_pad, F.Cu at (129.0, 57.7)
- added J25: Conn_01x01_Pin, smd_adapter:pin_pad, F.Cu at (129.0, 69.6)
- added J25: Conn_01x01_Pin, smd_adapter:pin_pad, F.Cu at (129.0, 121.3)
- added J25: Conn_01x01_Pin, smd_adapter:pin_pad, F.Cu at (129.0, 108.9)
- added J26: Conn_01x01_Pin, smd_adapter:pin_pad, F.Cu at (129.0, 123.8)
- added J26: Conn_01x01_Pin, smd_adapter:pin_pad, F.Cu at (129.0, 97.9)
- added J26: Conn_01x01_Pin, smd_adapter:pin_pad, F.Cu at (129.0, 72.2)
- added J26: Conn_01x01_Pin, smd_adapter:pin_pad, F.Cu at (129.0, 111.4)
- added J26: Conn_01x01_Pin, smd_adapter:pin_pad, F.Cu at (129.0, 60.2)
- added J26: Conn_01x01_Pin, smd_adapter:pin_pad, F.Cu at (129.0, 84.3)
- added J27: Conn_01x01_Pin, smd_adapter:pin_pad, F.Cu at (129.0, 86.8)
- added J27: Conn_01x01_Pin, smd_adapter:pin_pad, F.Cu at (129.0, 126.4)
- added J27: Conn_01x01_Pin, smd_adapter:pin_pad, F.Cu at (129.0, 74.7)
- added J27: Conn_01x01_Pin, smd_adapter:pin_pad, F.Cu at (129.0, 113.9)
- added J27: Conn_01x01_Pin, smd_adapter:pin_pad, F.Cu at (129.0, 62.8)
- added J27: Conn_01x01_Pin, smd_adapter:pin_pad, F.Cu at (129.0, 100.4)
- added J28: Conn_01x01_Pin, smd_adapter:pin_pad, F.Cu at (133.4, 70.9)
- added J28: Conn_01x01_Pin, smd_adapter:pin_pad, F.Cu at (133.4, 55.0)
- added J28: Conn_01x01_Pin, smd_adapter:pin_pad, F.Cu at (133.4, 86.8)
- added J28: Conn_01x01_Pin, smd_adapter:pin_pad, F.Cu at (133.4, 116.2)
- added J28: Conn_01x01_Pin, smd_adapter:pin_pad, F.Cu at (133.4, 102.0)
- added J29: Conn_01x01_Pin, smd_adapter:pin_pad, F.Cu at (133.4, 104.6)
- added J29: Conn_01x01_Pin, smd_adapter:pin_pad, F.Cu at (133.4, 118.7)
- added J29: Conn_01x01_Pin, smd_adapter:pin_pad, F.Cu at (133.4, 73.5)
- added J29: Conn_01x01_Pin, smd_adapter:pin_pad, F.Cu at (133.4, 89.3)
- added J29: Conn_01x01_Pin, smd_adapter:pin_pad, F.Cu at (133.4, 57.6)
- added J3: Conn_01x01_Pin, smd_adapter:pin_pad, F.Cu at (82.6, 96.2)
- added J3: Conn_01x01_Pin, smd_adapter:pin_pad, F.Cu at (82.6, 114.4)
- added J3: Conn_01x01_Pin, smd_adapter:pin_pad, F.Cu at (82.6, 75.0)
- added J3: Conn_01x01_Pin, smd_adapter:pin_pad, F.Cu at (82.6, 66.0)
- added J3: Conn_01x01_Pin, smd_adapter:pin_pad, F.Cu at (82.5, 123.8)
- added J3: Conn_01x01_Pin, smd_adapter:pin_pad, F.Cu at (82.6, 105.3)
- added J3: Conn_01x01_Pin, smd_adapter:pin_pad, F.Cu at (82.6, 85.1)
- added J30: Conn_01x01_Pin, smd_adapter:pin_pad, F.Cu at (133.4, 107.1)
- added J30: Conn_01x01_Pin, smd_adapter:pin_pad, F.Cu at (133.4, 91.9)
- added J30: Conn_01x01_Pin, smd_adapter:pin_pad, F.Cu at (133.4, 121.3)
- added J30: Conn_01x01_Pin, smd_adapter:pin_pad, F.Cu at (133.4, 60.1)
- added J30: Conn_01x01_Pin, smd_adapter:pin_pad, F.Cu at (133.4, 76.0)
- added J31: Conn_01x01_Pin, smd_adapter:pin_pad, F.Cu at (133.4, 109.7)
- added J31: Conn_01x01_Pin, smd_adapter:pin_pad, F.Cu at (133.4, 123.8)
- added J31: Conn_01x01_Pin, smd_adapter:pin_pad, F.Cu at (133.4, 94.4)
- added J31: Conn_01x01_Pin, smd_adapter:pin_pad, F.Cu at (133.4, 78.5)
- added J31: Conn_01x01_Pin, smd_adapter:pin_pad, F.Cu at (133.4, 62.7)
- added J32: Conn_01x01_Pin, smd_adapter:pin_pad, F.Cu at (133.4, 81.1)
- added J32: Conn_01x01_Pin, smd_adapter:pin_pad, F.Cu at (133.4, 126.4)
- added J32: Conn_01x01_Pin, smd_adapter:pin_pad, F.Cu at (133.4, 112.2)
- added J32: Conn_01x01_Pin, smd_adapter:pin_pad, F.Cu at (133.4, 65.2)
- added J32: Conn_01x01_Pin, smd_adapter:pin_pad, F.Cu at (133.4, 97.0)
- added J33: Conn_01x01_Pin, smd_adapter:pin_pad, F.Cu at (143.6, 55.0)
- added J33: Conn_01x01_Pin, smd_adapter:pin_pad, F.Cu at (143.6, 102.0)
- added J33: Conn_01x01_Pin, smd_adapter:pin_pad, F.Cu at (143.6, 116.2)
- added J33: Conn_01x01_Pin, smd_adapter:pin_pad, F.Cu at (143.6, 70.9)
- added J33: Conn_01x01_Pin, smd_adapter:pin_pad, F.Cu at (143.6, 86.8)
- added J34: Conn_01x01_Pin, smd_adapter:pin_pad, F.Cu at (143.6, 57.6)
- added J34: Conn_01x01_Pin, smd_adapter:pin_pad, F.Cu at (143.6, 118.7)
- added J34: Conn_01x01_Pin, smd_adapter:pin_pad, F.Cu at (143.6, 104.6)
- added J34: Conn_01x01_Pin, smd_adapter:pin_pad, F.Cu at (143.6, 89.3)
- added J34: Conn_01x01_Pin, smd_adapter:pin_pad, F.Cu at (143.6, 73.5)
- added J35: Conn_01x01_Pin, smd_adapter:pin_pad, F.Cu at (143.6, 60.1)
- added J35: Conn_01x01_Pin, smd_adapter:pin_pad, F.Cu at (143.6, 121.3)
- added J35: Conn_01x01_Pin, smd_adapter:pin_pad, F.Cu at (143.6, 91.9)
- added J35: Conn_01x01_Pin, smd_adapter:pin_pad, F.Cu at (143.6, 107.1)
- added J35: Conn_01x01_Pin, smd_adapter:pin_pad, F.Cu at (143.6, 76.0)
- added J36: Conn_01x01_Pin, smd_adapter:pin_pad, F.Cu at (143.6, 78.5)
- added J36: Conn_01x01_Pin, smd_adapter:pin_pad, F.Cu at (143.6, 109.7)
- added J36: Conn_01x01_Pin, smd_adapter:pin_pad, F.Cu at (143.6, 123.8)
- added J36: Conn_01x01_Pin, smd_adapter:pin_pad, F.Cu at (143.6, 62.7)
- added J36: Conn_01x01_Pin, smd_adapter:pin_pad, F.Cu at (143.6, 94.4)
- added J37: Conn_01x01_Pin, smd_adapter:pin_pad, F.Cu at (143.6, 112.2)
- added J37: Conn_01x01_Pin, smd_adapter:pin_pad, F.Cu at (143.6, 126.4)
- added J37: Conn_01x01_Pin, smd_adapter:pin_pad, F.Cu at (143.6, 97.0)
- added J37: Conn_01x01_Pin, smd_adapter:pin_pad, F.Cu at (143.6, 81.1)
- added J37: Conn_01x01_Pin, smd_adapter:pin_pad, F.Cu at (143.6, 65.2)
- added J4: Conn_01x01_Pin, smd_adapter:pin_pad, F.Cu at (82.6, 102.7)
- added J4: Conn_01x01_Pin, smd_adapter:pin_pad, F.Cu at (82.6, 111.8)
- added J4: Conn_01x01_Pin, smd_adapter:pin_pad, F.Cu at (82.6, 63.4)
- added J4: Conn_01x01_Pin, smd_adapter:pin_pad, F.Cu at (82.5, 121.2)
- added J4: Conn_01x01_Pin, smd_adapter:pin_pad, F.Cu at (82.6, 82.5)
- added J4: Conn_01x01_Pin, smd_adapter:pin_pad, F.Cu at (82.6, 72.5)
- added J4: Conn_01x01_Pin, smd_adapter:pin_pad, F.Cu at (82.6, 93.6)
- added J5: Conn_01x01_Pin, smd_adapter:pin_pad, F.Cu at (82.6, 87.6)
- added J5: Conn_01x01_Pin, smd_adapter:pin_pad, F.Cu at (82.6, 116.9)
- added J5: Conn_01x01_Pin, smd_adapter:pin_pad, F.Cu at (82.6, 68.5)
- added J5: Conn_01x01_Pin, smd_adapter:pin_pad, F.Cu at (82.6, 77.6)
- added J5: Conn_01x01_Pin, smd_adapter:pin_pad, F.Cu at (82.6, 98.7)
- added J5: Conn_01x01_Pin, smd_adapter:pin_pad, F.Cu at (82.5, 126.3)
- added J5: Conn_01x01_Pin, smd_adapter:pin_pad, F.Cu at (82.6, 107.8)
- added J6: Conn_01x01_Pin, smd_adapter:pin_pad, F.Cu at (103.5, 105.6)
- added J6: Conn_01x01_Pin, smd_adapter:pin_pad, F.Cu at (103.6, 55.0)
- added J6: Conn_01x01_Pin, smd_adapter:pin_pad, F.Cu at (103.6, 67.2)
- added J6: Conn_01x01_Pin, smd_adapter:pin_pad, F.Cu at (103.6, 92.6)
- added J6: Conn_01x01_Pin, smd_adapter:pin_pad, F.Cu at (103.6, 118.6)
- added J6: Conn_01x01_Pin, smd_adapter:pin_pad, F.Cu at (103.6, 79.9)
- added J7: Conn_01x01_Pin, smd_adapter:pin_pad, F.Cu at (103.6, 121.1)
- added J7: Conn_01x01_Pin, smd_adapter:pin_pad, F.Cu at (103.5, 108.1)
- added J7: Conn_01x01_Pin, smd_adapter:pin_pad, F.Cu at (103.6, 95.1)
- added J7: Conn_01x01_Pin, smd_adapter:pin_pad, F.Cu at (103.6, 69.7)
- added J7: Conn_01x01_Pin, smd_adapter:pin_pad, F.Cu at (103.6, 82.4)
- added J7: Conn_01x01_Pin, smd_adapter:pin_pad, F.Cu at (103.6, 57.6)
- added J8: Conn_01x01_Pin, smd_adapter:pin_pad, F.Cu at (103.6, 123.7)
- added J8: Conn_01x01_Pin, smd_adapter:pin_pad, F.Cu at (103.5, 110.7)
- added J8: Conn_01x01_Pin, smd_adapter:pin_pad, F.Cu at (103.6, 85.0)
- added J8: Conn_01x01_Pin, smd_adapter:pin_pad, F.Cu at (103.6, 97.7)
- added J8: Conn_01x01_Pin, smd_adapter:pin_pad, F.Cu at (103.6, 72.3)
- added J8: Conn_01x01_Pin, smd_adapter:pin_pad, F.Cu at (103.6, 60.1)
- added J9: Conn_01x01_Pin, smd_adapter:pin_pad, F.Cu at (103.5, 113.2)
- added J9: Conn_01x01_Pin, smd_adapter:pin_pad, F.Cu at (103.6, 74.8)
- added J9: Conn_01x01_Pin, smd_adapter:pin_pad, F.Cu at (103.6, 87.5)
- added J9: Conn_01x01_Pin, smd_adapter:pin_pad, F.Cu at (103.6, 100.2)
- added J9: Conn_01x01_Pin, smd_adapter:pin_pad, F.Cu at (103.6, 126.2)
- added J9: Conn_01x01_Pin, smd_adapter:pin_pad, F.Cu at (103.6, 62.7)
- added U1: SOIC8, smd_adapter:SOIC8, F.Cu at (108.9, 58.9)
- added U1: SOIC8, smd_adapter:SOIC8, F.Cu at (108.9, 71.0)
- added U1: SOIC8, smd_adapter:SOIC8, F.Cu at (108.9, 109.5)
- added U1: SOIC8, smd_adapter:SOIC8, F.Cu at (108.9, 122.5)
- added U1: SOIC8, smd_adapter:SOIC8, F.Cu at (108.9, 83.7)
- added U1: SOIC8, smd_adapter:SOIC8, F.Cu at (108.9, 96.4)
- added U2: SOT_32-5, smd_adapter:SOT-23-5, F.Cu at (85.6, 85.1)
- added U2: SOT_32-5, smd_adapter:SOT-23-5, F.Cu at (85.6, 114.3)
- added U2: SOT_32-5, smd_adapter:SOT-23-5, F.Cu at (85.5, 123.7)
- added U2: SOT_32-5, smd_adapter:SOT-23-5, F.Cu at (85.6, 75.0)
- added U2: SOT_32-5, smd_adapter:SOT-23-5, F.Cu at (85.6, 66.0)
- added U2: SOT_32-5, smd_adapter:SOT-23-5, F.Cu at (85.6, 105.3)
- added U2: SOT_32-5, smd_adapter:SOT-23-5, F.Cu at (85.6, 96.1)
- added U3: SOT_32-6, smd_adapter:SOT-23-6, F.Cu at (95.2, 67.1)
- added U3: SOT_32-6, smd_adapter:SOT-23-6, F.Cu at (95.2, 98.3)
- added U3: SOT_32-6, smd_adapter:SOT-23-6, F.Cu at (95.2, 87.5)
- added U3: SOT_32-6, smd_adapter:SOT-23-6, F.Cu at (95.2, 77.3)
- added U3: SOT_32-6, smd_adapter:SOT-23-6, F.Cu at (95.2, 123.8)
- added U3: SOT_32-6, smd_adapter:SOT-23-6, F.Cu at (95.2, 57.6)
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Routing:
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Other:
- board size 43.2 x 43.2 mm -> 63.9 x 74.2 mm
- board text added: "MSOP-8"
- board text added: "SOIC-8"
- board text added: "SOT23-5"
- board text added: "SOT23-6"
- board text added: "TSSOP-10"
- board text added: "V 0.1"
